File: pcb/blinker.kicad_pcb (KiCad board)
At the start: 2 copper layers, 55.9 x 55.9 mm, 15 parts, among them J1 ISP, U1 ATtiny10-TS

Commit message: Minor adjustments.
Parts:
- moved D2 2.07 mm to (156.7, 104.8)
- moved JP1 0.97 mm to (160.3, 104.7)
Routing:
- net 5VCC: track 42.1 -> 43.2 mm
- net 2.7VCC: track 16.0 -> 15.5 mm
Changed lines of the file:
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@@
   (net 10 "unconnected-(J1-Pad1)")
   (footprint "Diode_SMD:D_SOD-123" (layer "F.Cu")
-    (at 158.72 104.81 -90)
+    (at 156.65 104.82 -90)
     (descr "SOD-123")
     (tags "SOD-123")
@@
     (property "Sheetname" "")
     (attr smd)
-    (fp_text reference "D3" (at -6.54 -0.66) (layer "F.SilkS")
+    (fp_text reference "D3" (at -4.49 -1.36) (layer "F.SilkS")
       (effects (font (size 1 1) (thickness 0.15)))
     )
@@
   )
   (footprint "Jumper:SolderJumper-2_P1.3mm_Open_TrianglePad1.0x1.5mm" (layer "F.Cu")
-    (at 161.28 104.86 -90)
+    (at 160.32 104.72 -90)
     (descr "SMD Solder Jumper, 1x1.5mm Triangular Pads, 0.3mm gap, open")
     (tags "solder jumper open")
@@
     (effects (font (size 1.5 1.5) (thickness 0.3)) (justify mirror))
   )
-  (gr_text "ISP" (at 167.71 95.6 90) (layer "B.SilkS")
-    (effects (font (size 1.5 1.5) (thickness 0.3)) (justify mirror))
-  )
   (gr_text "+\n-" (at 155.37 98.82) (layer "B.SilkS")
     (effects (font (size 1.5 1.5) (thickness 0.3)) (justify mirror))
@@
     (effects (font (size 0.762 0.762) (thickness 0.127)))
   )
-  (gr_text "MORSE" (at 161.41 75.59) (layer "F.SilkS")
+  (gr_text "ISP" (at 166.88 108.66) (layer "F.SilkS")
+    (effects (font (size 1.5 1.5) (thickness 0.3)))
+  )
+  (gr_text "MORSE" (at 162.07 75.67) (layer "F.SilkS")
     (effects (font (size 0.762 0.762) (thickness 0.127)))
   )
   (gr_text "Love to Michelle, Alex and Sam" (at 165.67 110.86) (layer "F.SilkS")
+    (effects (font (size 1.5 1.5) (thickness 0.3)))
+  )
+  (gr_text "+\n-" (at 155.38 98.83) (layer "F.SilkS")
     (effects (font (size 1.5 1.5) (thickness 0.3)))
   )
@@
   (segment (start 164.89298 101.36298) (end 164.89298 99.523448) (width 0.25) (layer "F.Cu") (net 5))
   (segment (start 158.05 91.69) (end 158.05 88.971773) (width 0.25) (layer "F.Cu") (net 6))
-  (segment (start 160.305 103.16) (end 161.28 104.135) (width 0.25) (layer "F.Cu") (net 6))
+  (segment (start 151.42 103.16) (end 160.305 103.16) (width 0.25) (layer "F.Cu") (net 6))
+  (segment (start 160.305 103.16) (end 160.305 103.98) (width 0.25) (layer "F.Cu") (net 6))
+  (segment (start 149.86 101.6) (end 151.42 103.16) (width 0.25) (layer "F.Cu") (net 6))
   (segment (start 158.05 88.971773) (end 157.48 88.401773) (width 0.25) (layer "F.Cu") (net 6))
-  (segment (start 158.72 103.16) (end 160.305 103.16) (width 0.25) (layer "F.Cu") (net 6))
-  (segment (start 151.42 103.16) (end 149.86 101.6) (width 0.25) (layer "F.Cu") (net 6))
-  (segment (start 158.72 103.16) (end 151.42 103.16) (width 0.25) (layer "F.Cu") (net 6))
+  (segment (start 160.305 103.98) (end 160.32 103.995) (width 0.25) (layer "F.Cu") (net 6))
   (segment (start 165.69 81.29) (end 165.69 92.05) (width 0.25) (layer "F.Cu") (net 7))
   (segment (start 167.06 76.1825) (end 167.06 78.31) (width 0.25) (layer "F.Cu") (net 7))
@@
   (segment (start 167.06 79.92) (end 165.69 81.29) (width 0.25) (layer "F.Cu") (net 7))
   (segment (start 165.67 105.55899) (end 164.755521 104.644511) (width 0.25) (layer "F.Cu") (net 8))
-  (segment (start 161.64894 105.595) (end 161.39 105.595) (width 0.25) (layer "F.Cu") (net 8))
+  (segment (start 162.775489 104.644511) (end 162.599429 104.644511) (width 0.25) (layer "F.Cu") (net 8))
   (segment (start 165.67 106.531988) (end 165.67 105.55899) (width 0.25) (layer "F.Cu") (net 8))
   (segment (start 163.23 94.943217) (end 162.01 96.163217) (width 0.25) (layer "F.Cu") (net 8))
-  (segment (start 162.775489 104.644511) (end 162.599429 104.644511) (width 0.25) (layer "F.Cu") (net 8))
   (segment (start 162.775489 104.644511) (end 162.61798 104.487002) (width 0.25) (layer "F.Cu") (net 8))
   (segment (start 162.61798 104.487002) (end 162.61798 100.473448) (width 0.25) (layer "F.Cu") (net 8))
@@
   (segment (start 162.61798 100.473448) (end 163.221428 99.87) (width 0.25) (layer "F.Cu") (net 8))
   (segment (start 169.54 106.01) (end 168.365489 107.184511) (width 0.25) (layer "F.Cu") (net 8))
-  (segment (start 162.599429 104.644511) (end 161.64894 105.595) (width 0.25) (layer "F.Cu") (net 8))
   (segment (start 164.52 90.55) (end 163.23 91.84) (width 0.25) (layer "F.Cu") (net 8))
   (segment (start 163.221428 99.87) (end 162.01 98.658572) (width 0.25) (layer "F.Cu") (net 8))
+  (segment (start 162.599429 104.644511) (end 161.64894 105.595) (width 0.25) (layer "F.Cu") (net 8))
   (segment (start 164.52 76.0025) (end 164.52 78.31) (width 0.25) (layer "F.Cu") (net 8))
   (segment (start 163.605 99.87) (end 163.221428 99.87) (width 0.25) (layer "F.Cu") (net 8))
+  (segment (start 161.64894 105.595) (end 160.47 105.595) (width 0.25) (layer "F.Cu") (net 8))
   (segment (start 162.01 98.658572) (end 162.01 96.163217) (width 0.25) (layer "F.Cu") (net 8))
+  (segment (start 160.47 105.595) (end 160.32 105.445) (width 0.25) (layer "F.Cu") (net 8))
   (segment (start 164.9125 75.61) (end 164.52 76.0025) (width 0.25) (layer "F.Cu") (net 8))
   (segment (start 163.23 91.84) (end 163.23 94.943217) (width 0.25) (layer "F.Cu") (net 8))

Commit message: v1.2 of PCB
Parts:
- removed C3, C4, C5, C6: C_Polarized, Capacitor_THT:CP_Radial_D16.0mm_P7.50mm
- removed D2: D_Zener, Diode_SMD:D_SOD-123
- removed D4: LED, Connector_PinHeader_2.54mm:PinHeader_1x02_P2.54mm_Vertical
- SC1: moved to F.Cu
- moved D3 48.3 mm to (166.8, 123.8), turned to 0 degrees
- moved R1 28.2 mm to (166.8, 122.2), turned to 180 degrees
- moved D1 24.9 mm to (166.9, 116.0), turned to 90 degrees
- moved U1 24.1 mm to (175.2, 121.6)
- moved C1 17.4 mm to (171.6, 116.7)
- moved JP1 17.0 mm to (158.8, 121.6)
- moved SC1 14.9 mm to (165.9, 110.2), turned to 90 degrees
- moved J1 10.7 mm to (177.2, 110.9)
- moved C2 10.6 mm to (162.3, 116.7), turned to 180 degrees
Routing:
- net RESET: track 2.62 -> 26.9 mm
- net Net-(D3-Pad1): track 18.9 -> 1.71 mm
- net 5VCC: track 43.2 -> 34.7 mm
- net GND: track 0.00 -> 7.47 mm, vias 0 -> 2
- net TPICLK: track 5.67 -> 11.4 mm
- net TPIDATA: track 6.73 -> 10.8 mm
- net LED: track 4.38 -> 7.03 mm
- net /SLR_IN: track 3.77 -> 5.11 mm
- added copper zone on B.Cu, net GND
- removed copper zone on B.Cu, net 2.7VCC
- removed copper zone on F.Cu, net GND
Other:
- board size 55.9 x 55.9 mm -> 33.3 x 16.6 mm
- board text added: "v1.2"
- board text removed: "Blinker v1.1 CC0-1.0 License"
- board text removed: "CAP PWR"
- board text removed: "CODE"
- board text removed: "ISP"
- board text removed: "Love to Michelle, Alex and Sam"
- board text removed: "MORSE"
- board text removed: "SOL PNL"

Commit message: Making progress
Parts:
- removed R1: 220, Resistor_SMD:R_0603_1608Metric
- added C2: C_Polarized, Capacitor_THT:CP_Radial_D16.0mm_P7.50mm, B.Cu at (158.5, 113.1)
- added D10: WS2812B, LED_SMD:LED_Wurth_150044M155260, F.Cu at (147.8, 119.6)
- added D11: WS2812B, LED_SMD:LED_Wurth_150044M155260, F.Cu at (147.8, 117.7)
- added D12: WS2812B, LED_SMD:LED_Wurth_150044M155260, F.Cu at (147.8, 115.8)
- added D13: WS2812B, LED_SMD:LED_Wurth_150044M155260, F.Cu at (147.8, 113.9)
- added D2: WS2812B, LED_SMD:LED_Wurth_150044M155260, F.Cu at (151.6, 119.6)
- added D4: WS2812B, LED_SMD:LED_Wurth_150044M155260, F.Cu at (151.6, 115.8)
- added D5: WS2812B, LED_SMD:LED_Wurth_150044M155260, F.Cu at (151.6, 113.9)
- added D6: WS2812B, LED_SMD:LED_Wurth_150044M155260, F.Cu at (149.7, 119.6)
- added D7: WS2812B, LED_SMD:LED_Wurth_150044M155260, F.Cu at (149.7, 117.7)
- added D8: WS2812B, LED_SMD:LED_Wurth_150044M155260, F.Cu at (149.7, 115.8)
- added D9: WS2812B, LED_SMD:LED_Wurth_150044M155260, F.Cu at (149.7, 113.9)
- added JP2: Jumper_2_Open, Jumper:SolderJumper-2_P1.3mm_Open_TrianglePad1.0x1.5mm, F.Cu at (180.2, 133.8)
- added U2: M24C01-FDW, Package_SO:TSSOP-8_4.4x3mm_P0.65mm, F.Cu at (173.1, 139.6)
- D3: value LED -> WS2812B; footprint LED_SMD:LED_0603_1608Metric -> LED_SMD:LED_Wurth_150044M155260
- SC1: value Solar_Cell -> 3
- moved C2 21.0 mm to (141.6, 113.5), turned to -90 degrees
- moved D3 16.4 mm to (151.6, 117.7)
- moved J1 14.8 mm to (162.8, 114.4), turned to 0 degrees
- moved JP1 13.4 mm to (163.9, 134.0)
- moved U1 11.7 mm to (172.1, 132.8)
- moved C1 5.22 mm to (175.6, 113.3), turned to -90 degrees
- moved D1 4.19 mm to (171.1, 115.9)
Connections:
- net TPICLK renamed ROMSCL
- net TPIDATA renamed ROMSDA
- D3 pad 2: 5VCC -> Net-(D3-DOUT)
- U1 pad 4: LED -> LEDSTRING
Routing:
- net 5VCC: track 34.7 -> 0.00 mm
- net RESET: track 26.9 -> 0.00 mm
- net 2.7VCC: track 15.3 -> 0.00 mm
- net Net-(D5-DOUT): track 0.00 -> 12.0 mm, vias 0 -> 2
- net Net-(D10-DIN): track 0.00 -> 12.0 mm, vias 0 -> 2
- net ROMSCL: track 11.4 -> 0.00 mm
- net ROMSDA: track 10.8 -> 0.00 mm
- net LED: track 7.03 -> 0.00 mm
- net /SLR_IN: track 5.11 -> 0.00 mm
- net GND: track 7.47 -> 9.75 mm, vias 2 -> 0
- net Net-(D2-VDD): track 1.71 -> 0.00 mm
- net Net-(D12-DOUT): track 0.00 -> 1.45 mm
- net Net-(D8-DOUT): track 0.00 -> 1.44 mm
- net Net-(D2-DOUT): track 0.00 -> 1.44 mm
- net Net-(D6-DOUT): track 0.00 -> 1.44 mm
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- removed copper zone on B.Cu, net GND
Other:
- board outline removed
- board text added: "v2.0"
- board text removed: "v1.2"

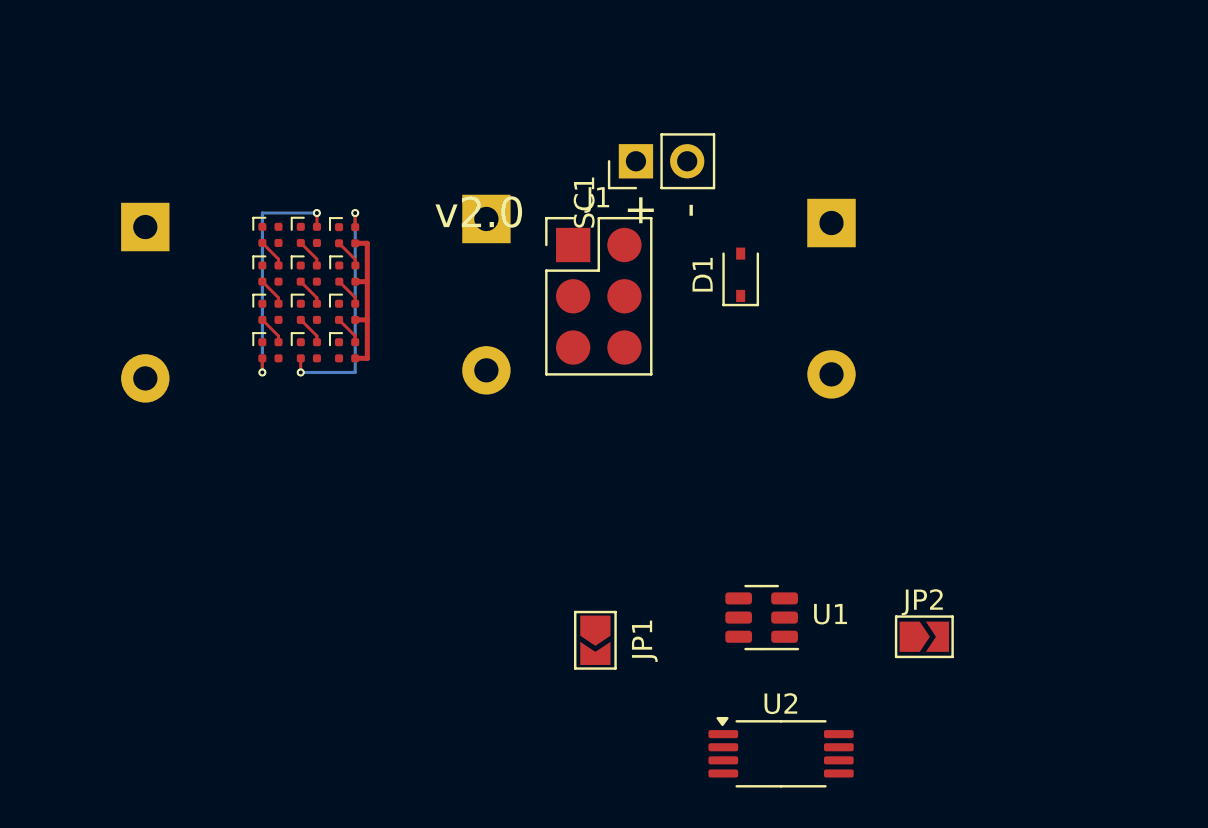
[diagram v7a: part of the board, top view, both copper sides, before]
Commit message: Adding decoupling caps and RC filter.
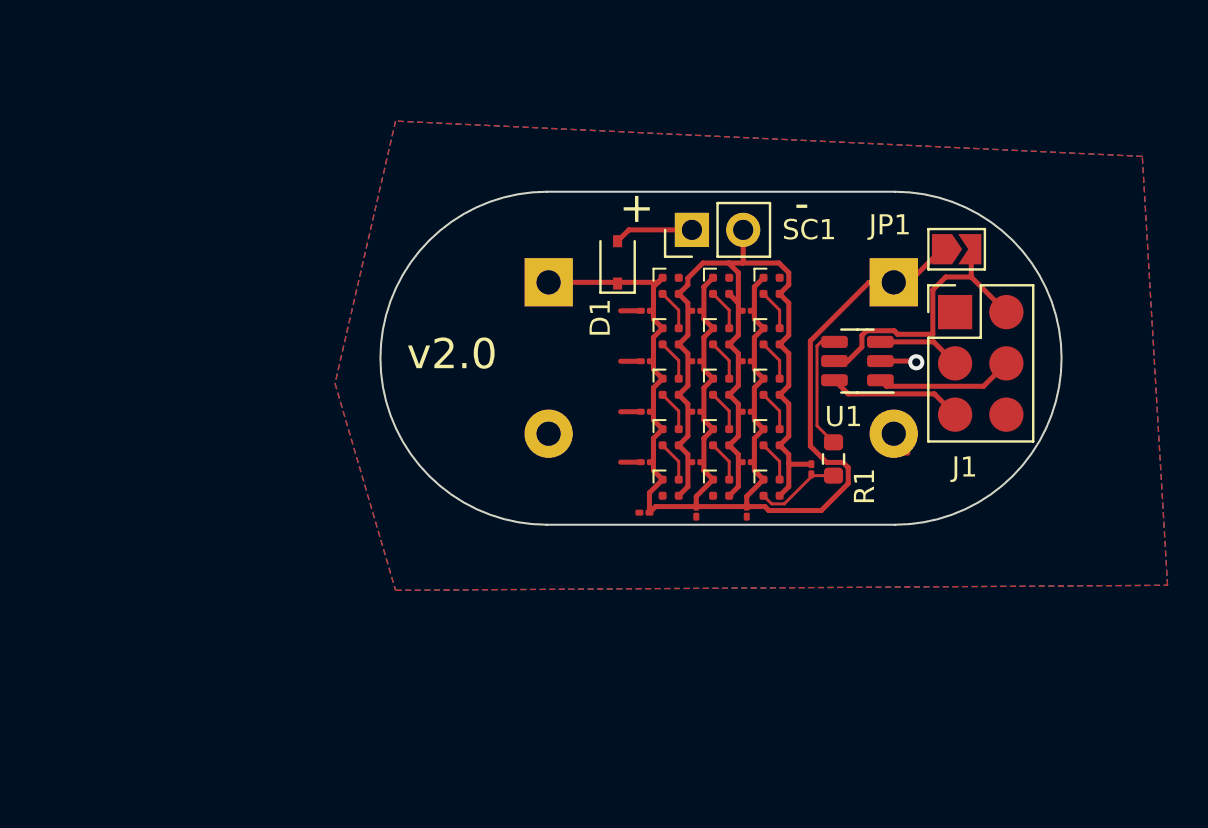
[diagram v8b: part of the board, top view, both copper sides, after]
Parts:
- removed the C2 at (141.6, 113.5)
- removed JP2: Jumper_2_Open, Jumper:SolderJumper-2_P1.3mm_Open_TrianglePad1.0x1.5mm
- removed U2: M24C01-FDW, Package_SO:TSSOP-8_4.4x3mm_P0.65mm
- added C10: 0.1uF, Capacitor_SMD:C_01005_0402Metric, F.Cu at (168.9, 122.7)
- added C11: 0.1uF, Capacitor_SMD:C_01005_0402Metric, F.Cu at (168.9, 125.2)
- added C12: 0.1uF, Capacitor_SMD:C_01005_0402Metric, F.Cu at (168.9, 127.6)
- added C13: 0.1uF, Capacitor_SMD:C_01005_0402Metric, F.Cu at (166.3, 127.7)
- added C14: 0.1uF, Capacitor_SMD:C_01005_0402Metric, F.Cu at (166.4, 125.2)
- added C15: 0.1uF, Capacitor_SMD:C_01005_0402Metric, F.Cu at (166.4, 122.7)
- added C16: 0.1uF, Capacitor_SMD:C_01005_0402Metric, F.Cu at (166.4, 120.2)
- added C17: 0.1uF, Capacitor_SMD:C_01005_0402Metric, F.Cu at (166.4, 117.7)
- added C18: 120 pF, Capacitor_SMD:C_01005_0402Metric, F.Cu at (174.6, 125.5)
- added C3: 0.1uF, Capacitor_SMD:C_01005_0402Metric, F.Cu at (171.4, 127.6)
- added C4: 0.1uF, Capacitor_SMD:C_01005_0402Metric, F.Cu at (171.4, 125.2)
- added C5: 0.1uF, Capacitor_SMD:C_01005_0402Metric, F.Cu at (171.4, 122.7)
- added C6: 0.1uF, Capacitor_SMD:C_01005_0402Metric, F.Cu at (171.4, 120.2)
- added C7: 0.1uF, Capacitor_SMD:C_01005_0402Metric, F.Cu at (171.4, 117.7)
- added C8: 0.1uF, Capacitor_SMD:C_01005_0402Metric, F.Cu at (168.9, 117.7)
- added C9: 0.1uF, Capacitor_SMD:C_01005_0402Metric, F.Cu at (168.9, 120.2)
- added D14: WS2812B, LED_SMD:LED_Wurth_150044M155260, F.Cu at (167.6, 121.4)
- added D15: WS2812B, LED_SMD:LED_Wurth_150044M155260, F.Cu at (167.6, 118.9)
- added D16: WS2812B, LED_SMD:LED_Wurth_150044M155260, F.Cu at (167.6, 116.4)
- added R1: 33Ω, Resistor_SMD:R_0603_1608Metric, F.Cu at (175.7, 125.0)
- moved JP1 26.4 mm to (181.8, 114.6), turned to 0 degrees
- moved D6 23.1 mm to (172.6, 116.4)
- moved D12 22.5 mm to (167.6, 126.4)
- moved D11 22.4 mm to (170.1, 116.4)
- moved D10 22.3 mm to (170.1, 118.9)
- moved D13 22.2 mm to (167.6, 123.9)
- moved D7 22.2 mm to (170.1, 126.4)
- moved D2 22.1 mm to (172.6, 126.4)
- moved D8 22.0 mm to (170.1, 123.9)
- moved D3 21.9 mm to (172.6, 123.9)
- moved D9 21.8 mm to (170.1, 121.4)
- moved D4 21.8 mm to (172.6, 121.4)
- moved D5 21.6 mm to (172.6, 118.9)
- moved J1 19.2 mm to (181.7, 117.7)
- moved U1 13.6 mm to (176.9, 120.1)
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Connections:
- C2 pad 1: (no net) -> 2.7VCC
- C2 pad 2: (no net) -> GND
- D10 pad 3: Net-(D10-VSS) -> GND
- D11 pad 3: Net-(D10-VSS) -> GND
- D12 pad 3: Net-(D10-VSS) -> GND
- D13 pad 2: unconnected-(D13-DOUT-Pad2) -> Net-(D13-DOUT)
- D13 pad 3: Net-(D10-VSS) -> GND
- D2 pad 1: Net-(D2-VDD) -> 2.7VCC
- D2 pad 4: LEDSTRING -> Net-(D2-DIN)
- D3 pad 1: Net-(D2-VDD) -> 2.7VCC
- D4 pad 1: Net-(D2-VDD) -> 2.7VCC
- D5 pad 1: Net-(D2-VDD) -> 2.7VCC
- D6 pad 1: Net-(D6-VDD) -> 2.7VCC
- D6 pad 3: Net-(D6-VSS) -> GND
- D7 pad 1: Net-(D6-VDD) -> 2.7VCC
- D7 pad 3: Net-(D6-VSS) -> GND
- D8 pad 1: Net-(D6-VDD) -> 2.7VCC
- D8 pad 3: Net-(D6-VSS) -> GND
- D9 pad 1: Net-(D6-VDD) -> 2.7VCC
- D9 pad 3: Net-(D6-VSS) -> GND
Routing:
- net 2.7VCC: track 0.00 -> 72.8 mm
- net GND: track 9.75 -> 54.7 mm, vias 0 -> 1
- net 5VCC: track 0.00 -> 14.1 mm
- net Net-(D5-DOUT): track 12.0 -> 2.03 mm, vias 2 -> 0
- net Net-(D10-DIN): track 12.0 -> 2.03 mm, vias 2 -> 0
- net ROMSDA: track 0.00 -> 6.84 mm
- net RESET: track 0.00 -> 6.69 mm
- net LEDSTRING: track 0.00 -> 6.06 mm
- net Net-(D2-DIN): track 0.00 -> 4.34 mm
- net ROMSCL: track 0.00 -> 4.15 mm
- net /SLR_IN: track 0.00 -> 3.92 mm
- net Net-(D15-DOUT): track 0.00 -> 2.03 mm
- net Net-(D14-DOUT): track 0.00 -> 2.03 mm
- net Net-(D13-DOUT): track 0.00 -> 2.03 mm
- net Net-(D6-DOUT): track 1.44 -> 0.00 mm
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- added copper zone on B.Cu, net GND
- added copper zone on F.Cu, net GND
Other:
- board outline added: 33.8 x 16.5 mm
- board text added: "+"
- board text added: "-"
- board text removed: "+ -"
